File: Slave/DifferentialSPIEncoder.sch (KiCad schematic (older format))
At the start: 31 parts, among them J1 Debug, J2 8P8C_LED_Shielded, U2 AS5048A, U3 SN65HVD06D, U4 SN65HVD06D, U5 SN65HVD06D

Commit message: Tweaks to layout to better fit AMT footprint
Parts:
- H1, H2: footprint MountingHole:MountingHole_3.2mm_M3 -> MountingHole:MountingHole_3mm
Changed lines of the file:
@@
 F 0 "H1" H 6500 6596 50  0000 L CNN
 F 1 "MountingHole" H 6500 6505 50  0000 L CNN
-F 2 "MountingHole:MountingHole_3.2mm_M3" H 6400 6550 50  0001 C CNN
+F 2 "MountingHole:MountingHole_3mm" H 6400 6550 50  0001 C CNN
 F 3 "~" H 6400 6550 50  0001 C CNN
 	1    6400 6550
@@
 F 0 "H2" H 6700 6596 50  0000 L CNN
 F 1 "MountingHole" H 6700 6505 50  0000 L CNN
-F 2 "MountingHole:MountingHole_3.2mm_M3" H 6600 6550 50  0001 C CNN
+F 2 "MountingHole:MountingHole_3mm" H 6600 6550 50  0001 C CNN
 F 3 "~" H 6600 6550 50  0001 C CNN
 	1    6600 6550

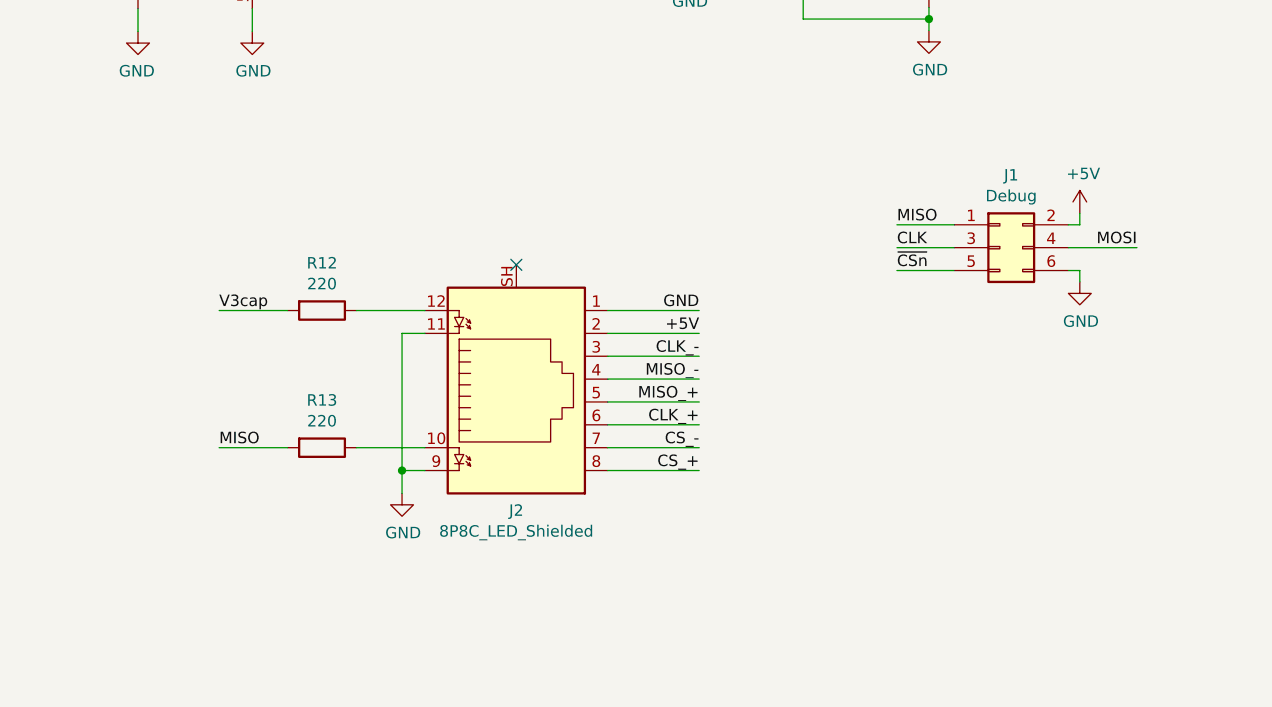
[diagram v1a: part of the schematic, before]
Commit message: Add silkscreen with info
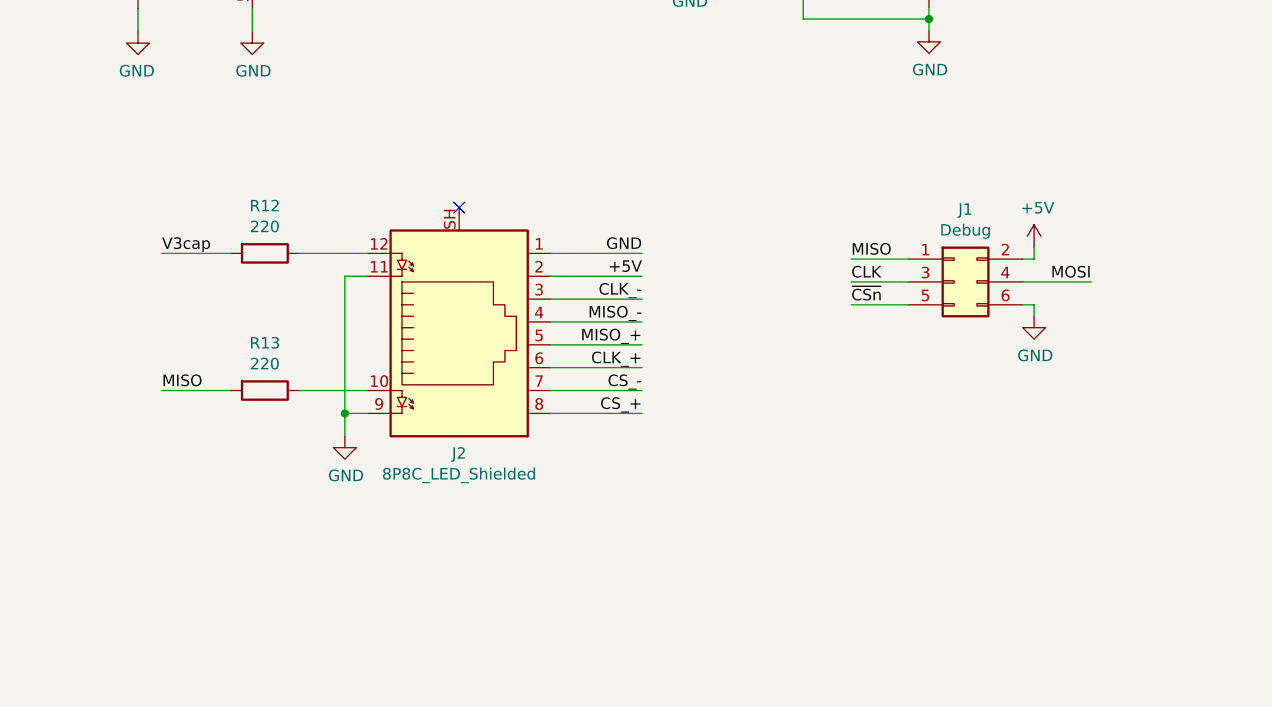
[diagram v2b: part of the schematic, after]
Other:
- moved on the sheet: J1, J2, R12, R13
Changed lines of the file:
@@
 Comment4 ""
 $EndDescr
-NoConn ~ 5700 3250
-Wire Wire Line
-	6500 3450 6100 3450
-Wire Wire Line
-	6100 4150 6500 4150
-Wire Wire Line
-	6100 4050 6500 4050
-Wire Wire Line
-	6100 3950 6500 3950
-Wire Wire Line
-	6100 3850 6500 3850
-Wire Wire Line
-	6100 3750 6500 3750
-Text Label 6500 4150 2    50   ~ 0
+NoConn ~ 5450 3000
+Wire Wire Line
+	6250 3200 5850 3200
+Wire Wire Line
+	5850 3900 6250 3900
+Wire Wire Line
+	5850 3800 6250 3800
+Wire Wire Line
+	5850 3700 6250 3700
+Wire Wire Line
+	5850 3600 6250 3600
+Wire Wire Line
+	5850 3500 6250 3500
+Text Label 6250 3900 2    50   ~ 0
 CS_+
-Text Label 6500 4050 2    50   ~ 0
+Text Label 6250 3800 2    50   ~ 0
 CS_-
-Text Label 6500 3950 2    50   ~ 0
+Text Label 6250 3700 2    50   ~ 0
 CLK_+
-Text Label 6500 3850 2    50   ~ 0
+Text Label 6250 3600 2    50   ~ 0
 MISO_+
-Text Label 6500 3750 2    50   ~ 0
+Text Label 6250 3500 2    50   ~ 0
 MISO_-
 Wire Wire Line
-	6500 3650 6100 3650
-Text Label 6500 3650 2    50   ~ 0
+	6250 3400 5850 3400
+Text Label 6250 3400 2    50   ~ 0
 CLK_-
 Wire Wire Line
-	6500 3550 6100 3550
-Text Label 6500 3550 2    50   ~ 0
+	6250 3300 5850 3300
+Text Label 6250 3300 2    50   ~ 0
 +5V
 $Comp
 L Connector:8P8C_LED_Shielded J2
 U 1 1 5DEFE4D2
-P 5700 3750
-F 0 "J2" H 5700 4325 50  0000 C CNN
-F 1 "8P8C_LED_Shielded" H 5700 4416 50  0000 C CNN
-F 2 "Connector_RJ:RJ45_Amphenol_RJHSE538X" V 5700 3775 50  0001 C CNN
-F 3 "~" V 5700 3775 50  0001 C CNN
-	1    5700 3750
+P 5450 3500
+F 0 "J2" H 5450 4075 50  0000 C CNN
+F 1 "8P8C_LED_Shielded" H 5450 4166 50  0000 C CNN
+F 2 "Connector_RJ:RJ45_Amphenol_RJHSE538X" V 5450 3525 50  0001 C CNN
+F 3 "~" V 5450 3525 50  0001 C CNN
+	1    5450 3500
 	1    0    0    1
 $EndComp
@@
 L power:GND #PWR0113
 U 1 1 5DEACD41
-P 8165 3325
-F 0 "#PWR0113" H 8165 3075 50  0001 C CNN
-F 1 "GND" H 8170 3152 50  0000 C CNN
-F 2 "" H 8165 3325 50  0001 C CNN
-F 3 "" H 8165 3325 50  0001 C CNN
-	1    8165 3325
-	1    0    0    -1
-$EndComp
-Wire Wire Line
-	8165 3325 8165 3275
-Wire Wire Line
-	8165 3275 8115 3275
-Text Label 8415 3175 2    50   ~ 0
+P 7965 3475
+F 0 "#PWR0113" H 7965 3225 50  0001 C CNN
+F 1 "GND" H 7970 3302 50  0000 C CNN
+F 2 "" H 7965 3475 50  0001 C CNN
+F 3 "" H 7965 3475 50  0001 C CNN
+	1    7965 3475
+	1    0    0    -1
+$EndComp
+Wire Wire Line
+	7965 3475 7965 3425
+Wire Wire Line
+	7965 3425 7915 3425
+Text Label 8215 3325 2    50   ~ 0
 MOSI
 Wire Wire Line
-	8415 3175 8115 3175
+	8215 3325 7915 3325
 $Comp
 L power:+5V #PWR0112
 U 1 1 5DEBDB96
-P 8165 3025
-F 0 "#PWR0112" H 8165 2875 50  0001 C CNN
-F 1 "+5V" H 8180 3198 50  0000 C CNN
-F 2 "" H 8165 3025 50  0001 C CNN
-F 3 "" H 8165 3025 50  0001 C CNN
-	1    8165 3025
-	1    0    0    -1
-$EndComp
-Wire Wire Line
-	8165 3025 8165 3075
-Wire Wire Line
-	8165 3075 8115 3075
+P 7965 3175
+F 0 "#PWR0112" H 7965 3025 50  0001 C CNN
+F 1 "+5V" H 7980 3348 50  0000 C CNN
+F 2 "" H 7965 3175 50  0001 C CNN
+F 3 "" H 7965 3175 50  0001 C CNN
+	1    7965 3175
+	1    0    0    -1
+$EndComp
+Wire Wire Line
+	7965 3175 7965 3225
+Wire Wire Line
+	7965 3225 7915 3225
 Wire Wire Line
 	5030 1730 4945 1730
@@
 $EndComp
 Wire Wire Line
-	7365 3275 7615 3275
-Wire Wire Line
-	7365 3175 7615 3175
-Wire Wire Line
-	7365 3075 7615 3075
-Text Label 7365 3275 0    50   ~ 0
+	7165 3425 7415 3425
+Wire Wire Line
+	7165 3325 7415 3325
+Wire Wire Line
+	7165 3225 7415 3225
+Text Label 7165 3425 0    50   ~ 0
 ~CSn
-Text Label 7365 3175 0    50   ~ 0
+Text Label 7165 3325 0    50   ~ 0
 CLK
-Text Label 7365 3075 0    50   ~ 0
+Text Label 7165 3225 0    50   ~ 0
 MISO
 NoConn ~ 1950 4060
@@
 L Device:R R12
 U 1 1 5DFC94D7
-P 4850 3450
-F 0 "R12" V 4643 3450 50  0000 C CNN
-F 1 "220" V 4734 3450 50  0000 C CNN
-F 2 "Resistor_SMD:R_0402_1005Metric" V 4780 3450 50  0001 C CNN
-F 3 "https://www.mouser.com/ProductDetail/Yageo/AA0402FR-071KL?qs=sGAEpiMZZMu61qfTUdNhG13ofUK0W8CzKiNWDYwkGfJyivaq%252BN2HvQ%3D%3D" H 4850 3450 50  0001 C CNN
-F 4 "Yageo" H 4850 3450 50  0001 C CNN "MANUFACTURER"
-F 5 "AA0402FR-071KL" H 4850 3450 50  0001 C CNN "MFN"
-	1    4850 3450
+P 4600 3200
+F 0 "R12" V 4393 3200 50  0000 C CNN
+F 1 "220" V 4484 3200 50  0000 C CNN
+F 2 "Resistor_SMD:R_0402_1005Metric" V 4530 3200 50  0001 C CNN
+F 3 "https://www.mouser.com/ProductDetail/Yageo/AA0402FR-071KL?qs=sGAEpiMZZMu61qfTUdNhG13ofUK0W8CzKiNWDYwkGfJyivaq%252BN2HvQ%3D%3D" H 4600 3200 50  0001 C CNN
+F 4 "Yageo" H 4600 3200 50  0001 C CNN "MANUFACTURER"
+F 5 "AA0402FR-071KL" H 4600 3200 50  0001 C CNN "MFN"
+	1    4600 3200
 	0    1    1    0
 $EndComp
 Wire Wire Line
-	5000 3450 5300 3450
+	4750 3200 5050 3200
 $Comp
 L Device:R R13
 U 1 1 5DFE18FA
-P 4850 4050
-F 0 "R13" V 4643 4050 50  0000 C CNN
-F 1 "220" V 4734 4050 50  0000 C CNN
-F 2 "Resistor_SMD:R_0402_1005Metric" V 4780 4050 50  0001 C CNN
-F 3 "https://www.mouser.com/ProductDetail/Yageo/AA0402FR-071KL?qs=sGAEpiMZZMu61qfTUdNhG13ofUK0W8CzKiNWDYwkGfJyivaq%252BN2HvQ%3D%3D" H 4850 4050 50  0001 C CNN
-F 4 "Yageo" H 4850 4050 50  0001 C CNN "MANUFACTURER"
-F 5 "AA0402FR-071KL" H 4850 4050 50  0001 C CNN "MFN"
-	1    4850 4050
+P 4600 3800
+F 0 "R13" V 4393 3800 50  0000 C CNN
+F 1 "220" V 4484 3800 50  0000 C CNN
+F 2 "Resistor_SMD:R_0402_1005Metric" V 4530 3800 50  0001 C CNN
+F 3 "https://www.mouser.com/ProductDetail/Yageo/AA0402FR-071KL?qs=sGAEpiMZZMu61qfTUdNhG13ofUK0W8CzKiNWDYwkGfJyivaq%252BN2HvQ%3D%3D" H 4600 3800 50  0001 C CNN
+F 4 "Yageo" H 4600 3800 50  0001 C CNN "MANUFACTURER"
+F 5 "AA0402FR-071KL" H 4600 3800 50  0001 C CNN "MFN"
+	1    4600 3800
 	0    1    1    0
 $EndComp
 Wire Wire Line
-	5000 4050 5300 4050
-Wire Wire Line
-	4700 4050 4400 4050
-Wire Wire Line
-	4400 3450 4700 3450
-Text Label 4400 4050 0    50   ~ 0
+	4750 3800 5050 3800
+Wire Wire Line
+	4450 3800 4150 3800
+Wire Wire Line
+	4150 3200 4450 3200
+Text Label 4150 3800 0    50   ~ 0
 MISO
-Text Label 4400 3450 0    50   ~ 0
+Text Label 4150 3200 0    50   ~ 0
 V3cap
 $Comp
 L power:GND #PWR03
 U 1 1 5E017234
-P 5200 4250
-F 0 "#PWR03" H 5200 4000 50  0001 C CNN
-F 1 "GND" H 5205 4077 50  0000 C CNN
-F 2 "" H 5200 4250 50  0001 C CNN
-F 3 "" H 5200 4250 50  0001 C CNN
-	1    5200 4250
-	1    0    0    -1
-$EndComp
-Wire Wire Line
-	5200 4250 5200 4150
-Wire Wire Line
-	5200 4150 5300 4150
-Wire Wire Line
-	5200 4150 5200 3550
-Wire Wire Line
-	5200 3550 5300 3550
-Connection ~ 5200 4150
-Text Label 6500 3450 2    50   ~ 0
+P 4950 4000
+F 0 "#PWR03" H 4950 3750 50  0001 C CNN
+F 1 "GND" H 4955 3827 50  0000 C CNN
+F 2 "" H 4950 4000 50  0001 C CNN
+F 3 "" H 4950 4000 50  0001 C CNN
+	1    4950 4000
+	1    0    0    -1
+$EndComp
+Wire Wire Line
+	4950 4000 4950 3900
+Wire Wire Line
+	4950 3900 5050 3900
+Wire Wire Line
+	4950 3900 4950 3300
+Wire Wire Line
+	4950 3300 5050 3300
+Connection ~ 4950 3900
+Text Label 6250 3200 2    50   ~ 0
 GND
 $Comp
@@
 L Connector_Generic:Conn_02x03_Odd_Even J1
 U 1 1 5DE9B749
-P 7815 3175
-F 0 "J1" H 7865 3492 50  0000 C CNN
-F 1 "Debug" H 7865 3401 50  0000 C CNN
-F 2 "Connector_PinHeader_2.54mm:PinHeader_2x03_P2.54mm_Vertical" H 7815 3175 50  0001 C CNN
-F 3 "~" H 7815 3175 50  0001 C CNN
-	1    7815 3175
-	1    0    0    -1
-$EndComp
+P 7615 3325
+F 0 "J1" H 7665 3642 50  0000 C CNN
+F 1 "Debug" H 7665 3551 50  0000 C CNN
+F 2 "Connector_PinHeader_2.54mm:PinHeader_2x03_P2.54mm_Vertical" H 7615 3325 50  0001 C CNN
+F 3 "~" H 7615 3325 50  0001 C CNN
+	1    7615 3325
+	1    0    0    -1
+$EndComp

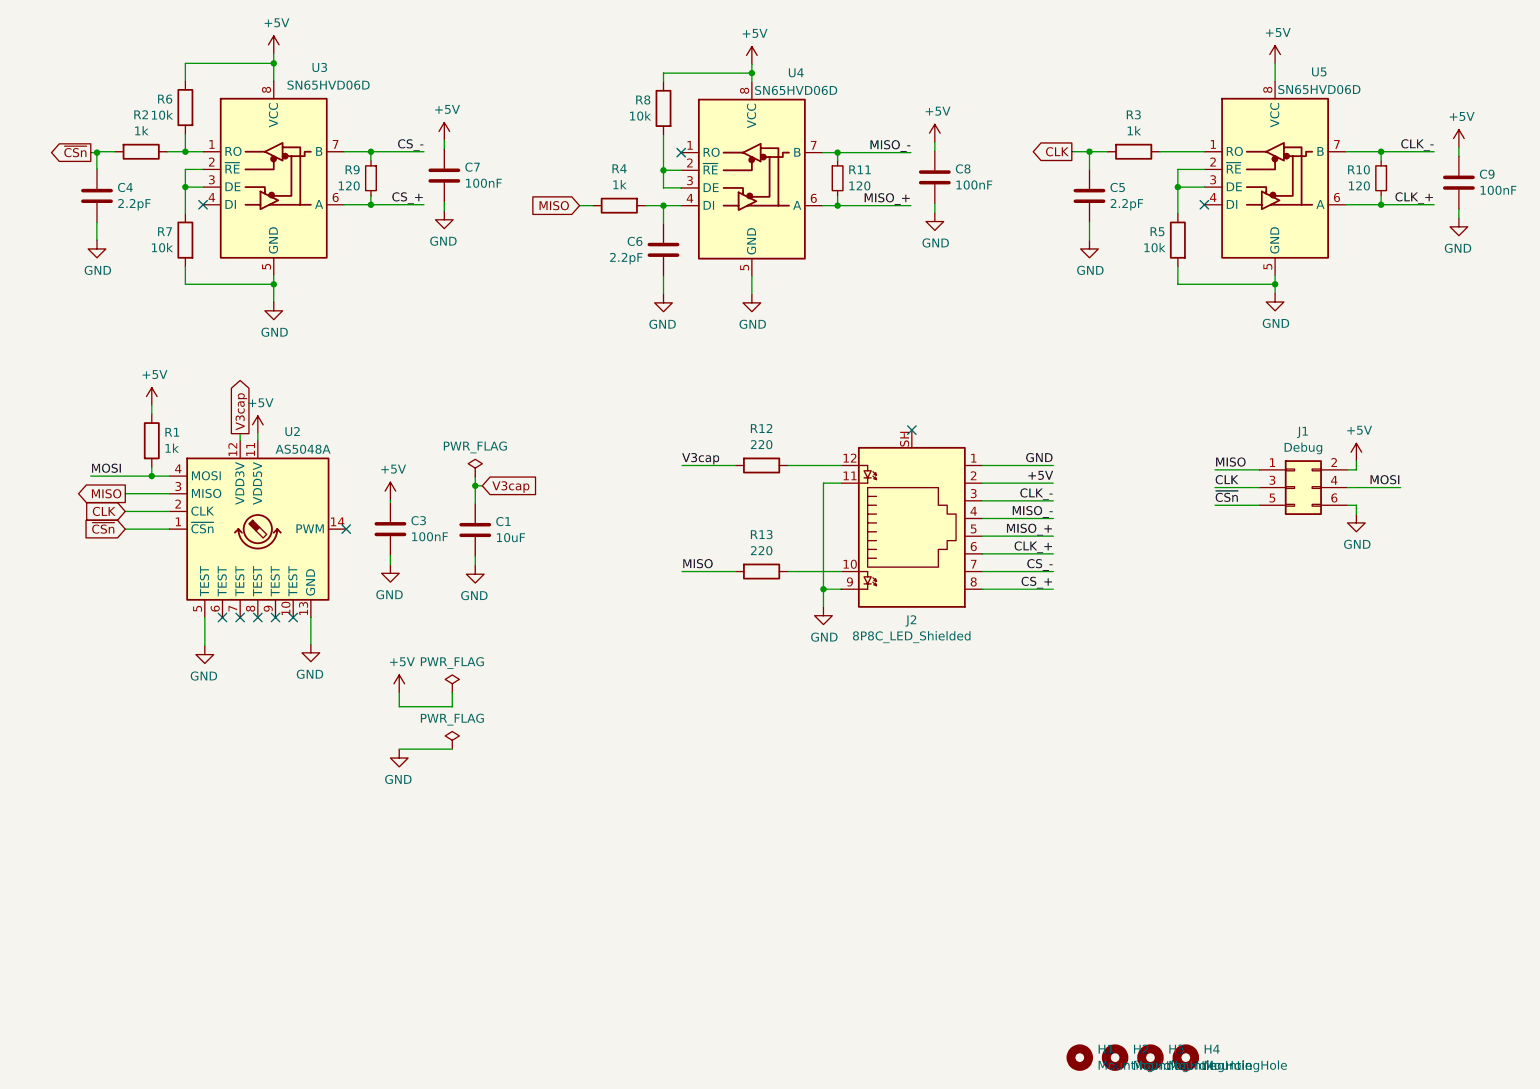
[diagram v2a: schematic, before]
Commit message: Swap AS5048A with AS5047U
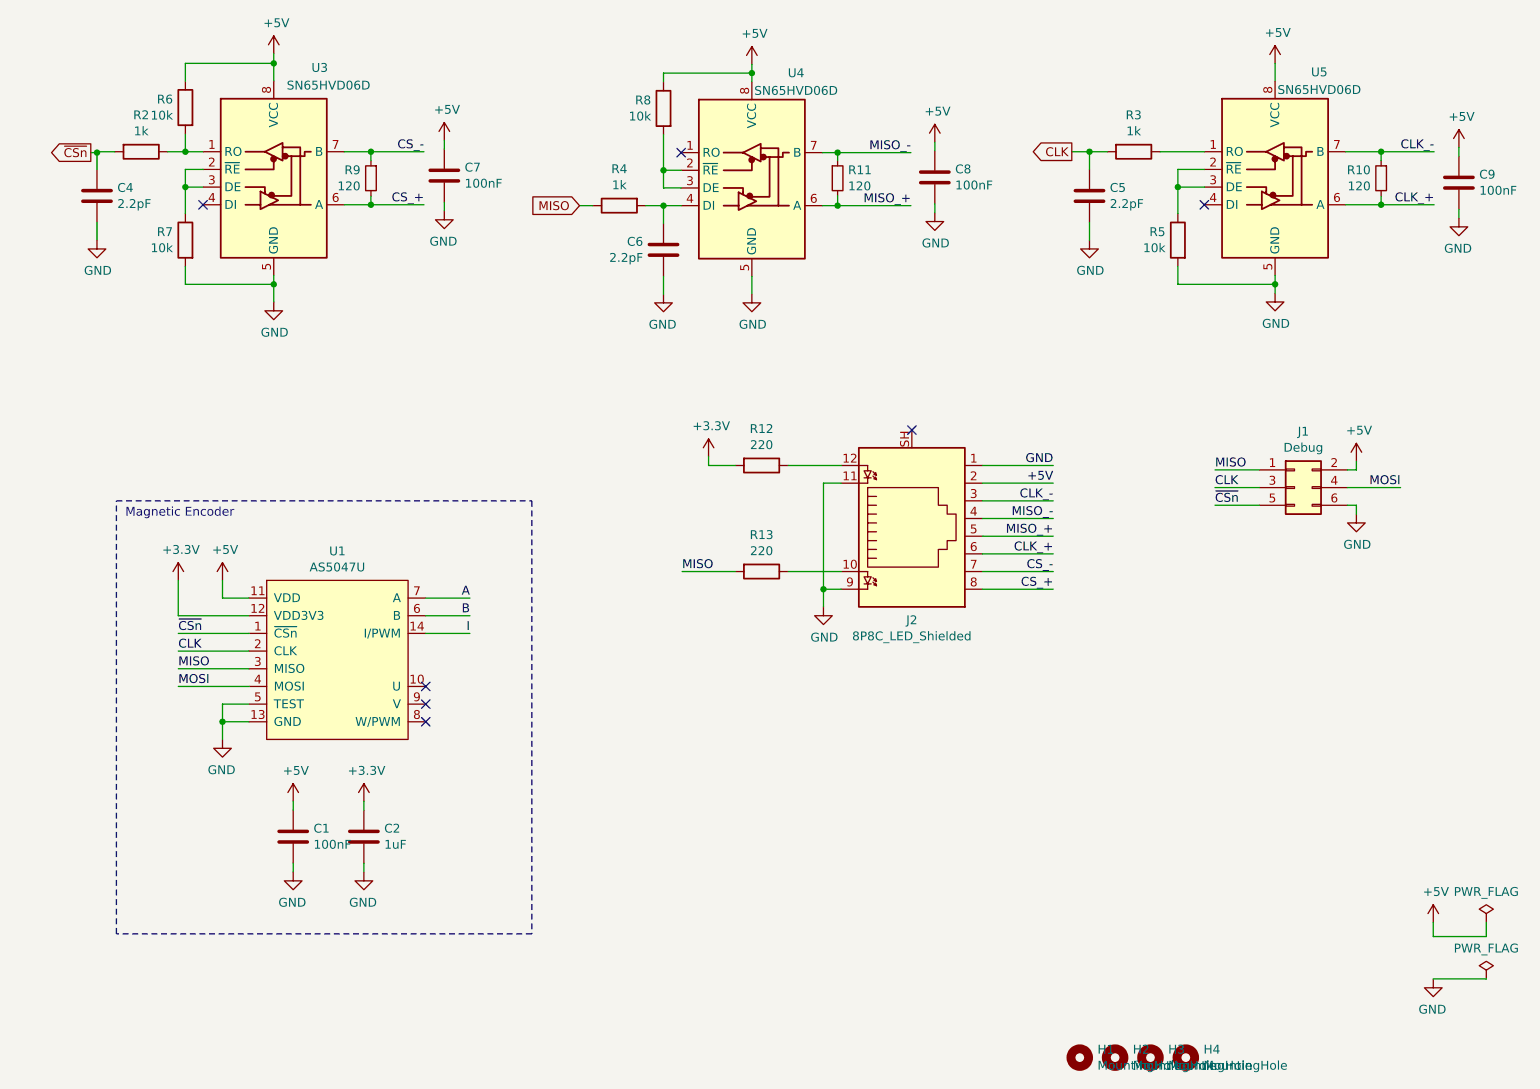
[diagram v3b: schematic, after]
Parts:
- removed C3: 100nF, Capacitor_SMD:C_0402_1005Metric, symbol Device:C
- removed R1: 1k, Resistor_SMD:R_0402_1005Metric, symbol Device:R
- removed U2: AS5048A, Package_SO:TSSOP-14_4.4x5mm_P0.65mm, symbol Sensor_Magnetic:AS5048A
- added C2: 1uF, Capacitor_SMD:C_0603_1608Metric, symbol Device:C
- added U1: AS5047U, Package_SO:TSSOP-14_4.4x5mm_P0.65mm, symbol Wetmelon:AS5047U
- C1: value 10uF -> 100nF; footprint Capacitor_SMD:C_0603_1608Metric -> Capacitor_SMD:C_0402_1005Metric; MFN C0603C106M8PACTU -> C0402C104K8PAC7411
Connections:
- net +5V: now also C1.1, U1.11 (VDD)
- net CLK: now also U1.2 (CLK)
- net GND: now also C2.2, U1.13 (GND), U1.5 (TEST)
- net MISO: now also U1.3 (MISO)
- net MOSI: now also U1.4 (MOSI)
- net ~CSn: now also U1.1 (~CSn)
- net V3cap renamed +3V3
- net +3V3: now also C2.1, U1.12 (VDD3V3); no longer C1.1
- new net A: U1.7 (A)
- new net B: U1.6 (B)
- new net I: U1.14 (I/PWM)
- no-connect marks 10 -> 7
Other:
- note added: "Magnetic Encoder"
